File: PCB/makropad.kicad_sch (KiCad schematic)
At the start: 46 parts, among them J1 OLED_DISPLAY, J2 Conn_01x04, SW1 SW_Push_45deg, SW10 SW_Push_45deg, SW11 RotaryEncoder_Switch, SW12 RotaryEncoder_Switch, SW2 SW_Push_45deg, SW3 SW_Push_45deg, SW4 SW_Push_45deg, SW5 SW_Push_45deg, SW6 SW_Push_45deg, SW7 SW_Push_45deg, SW8 SW_Push_45deg, SW9 SW_Push_45deg, U1 PCF8574A, U2 MOUDLE-SEEEDUINO-XIAO

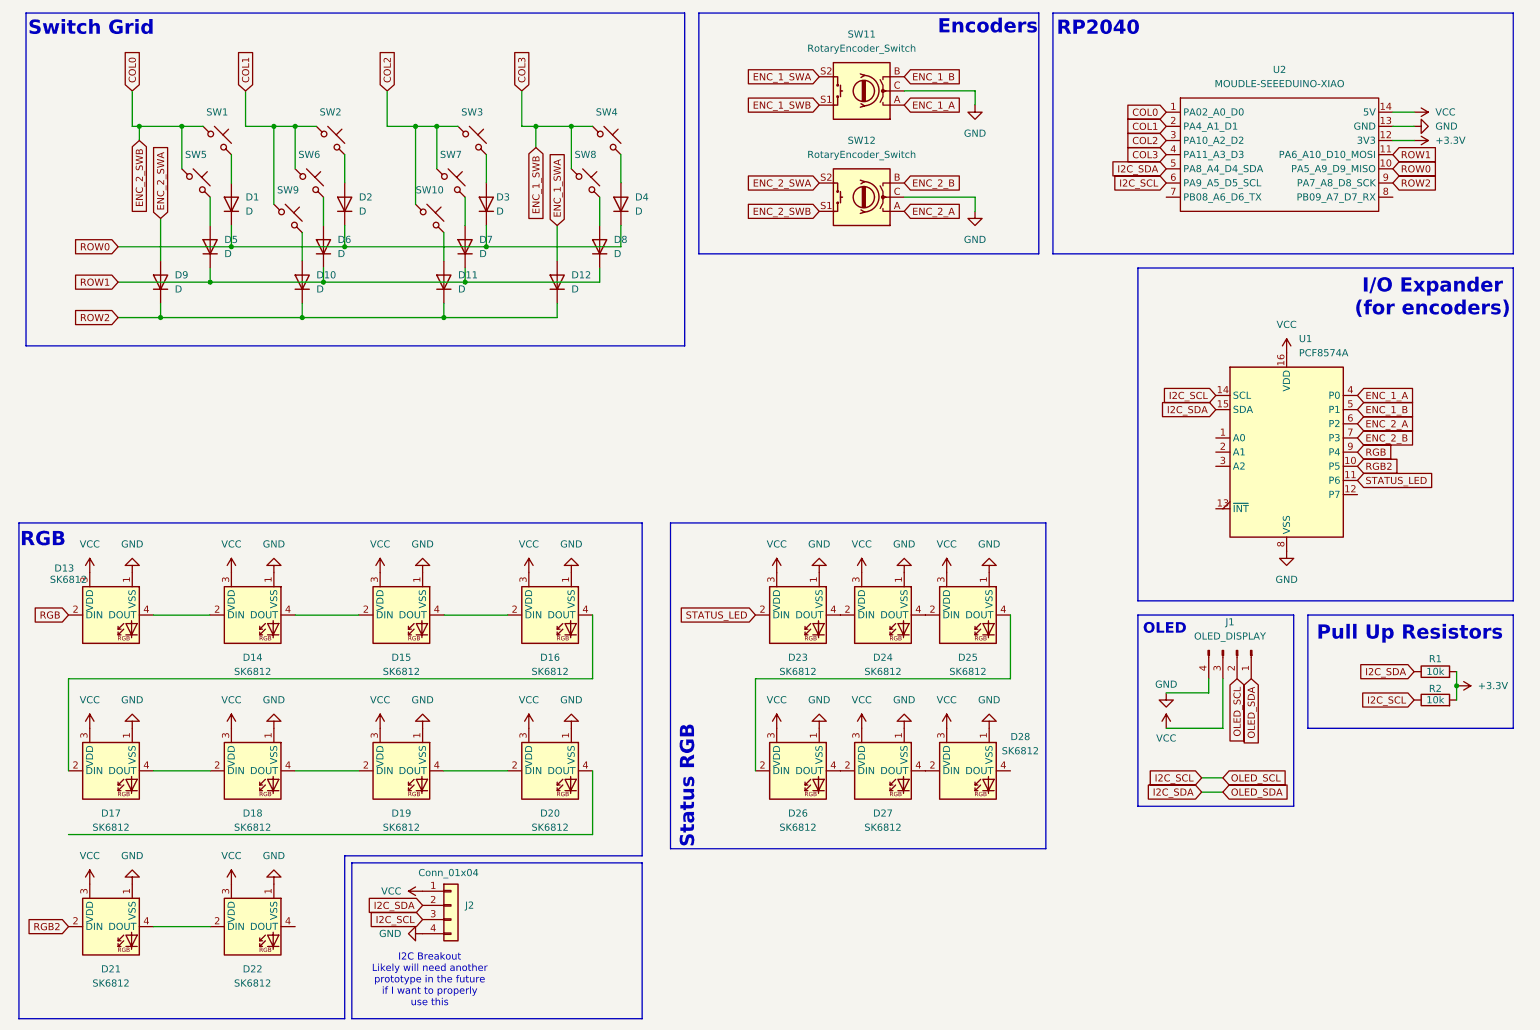
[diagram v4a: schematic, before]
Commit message: finally finish up pcb and fix led wiring
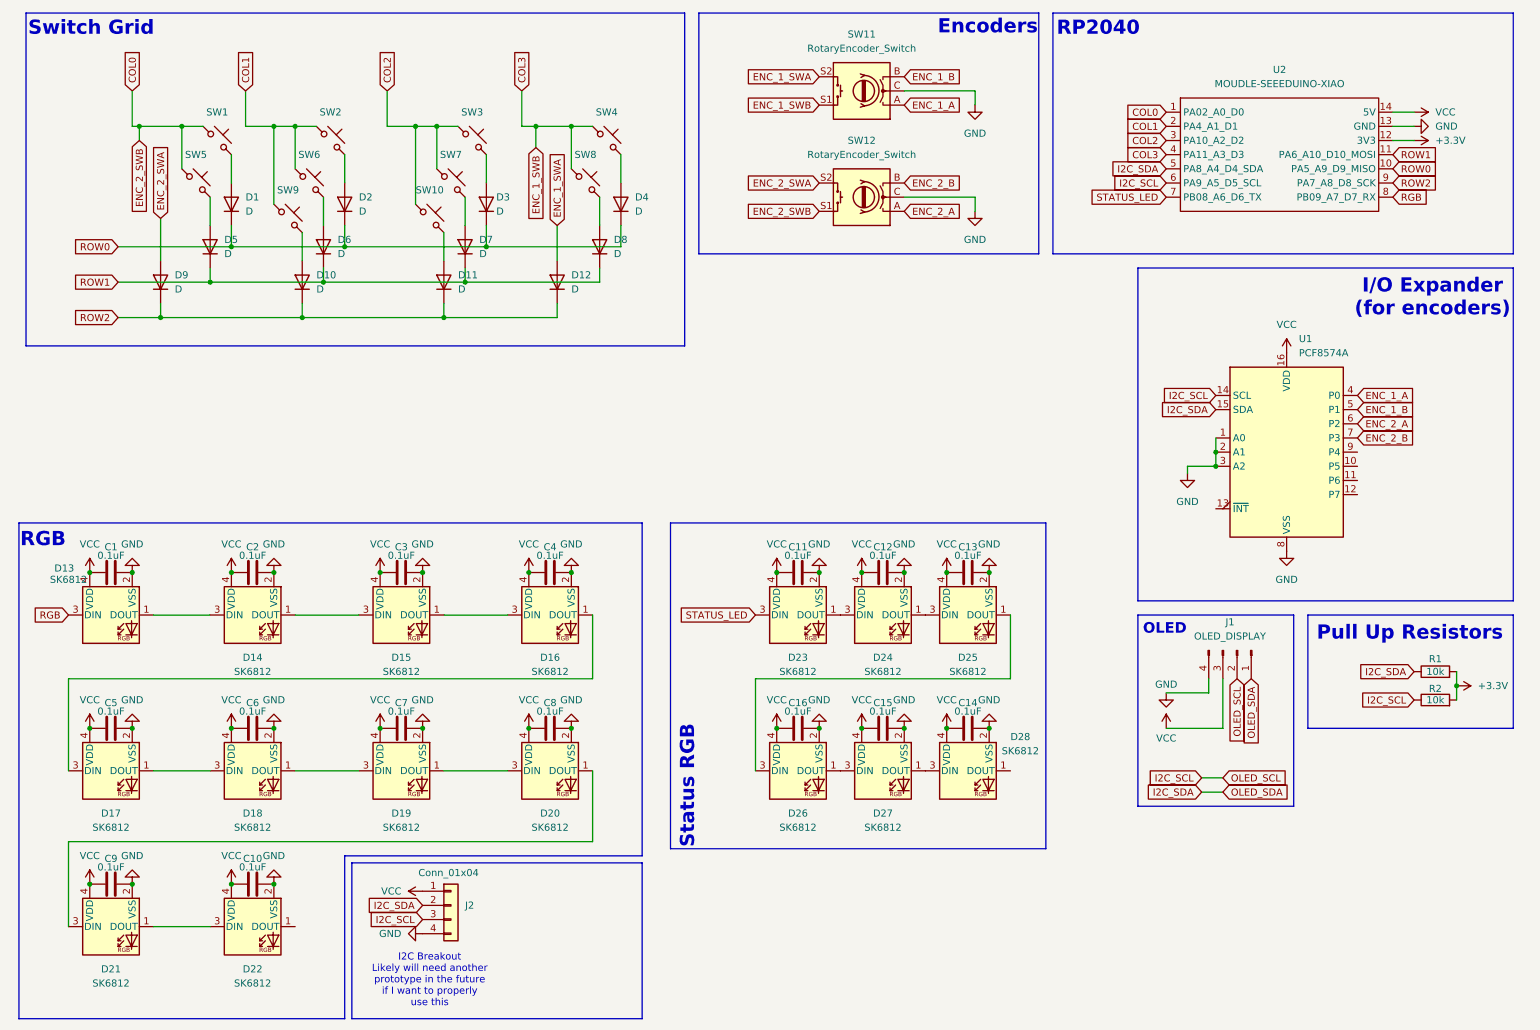
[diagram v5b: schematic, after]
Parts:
- added C1, C10, C11, C12, C13, C14, C15, C16, C2, C3, C4, C5, C6, C7, C8, C9: 0.1uF, Capacitor_SMD:C_1206_3216Metric, symbol Device:C
- D13, D14, D15, D16, D17, D18, D19, D20, D21, D22: footprint Components:LED_SK6812MINI -> neopixel.petty:SK6812MINI-E; symbol SK6812_CUSTOM:SK6812_Custom -> neopixel:SK6812MINI
- D23, D24, D25, D26, D27, D28: footprint LED_SMD:LED_SK6812_PLCC4_5.0x5.0mm_P3.2mm -> LED_SMD:LED_SK6812MINI_PLCC4_3.5x3.5mm_P1.75mm; symbol SK6812_CUSTOM:SK6812_Custom -> neopixel:SK6812MINI
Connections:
- net GND: now also D13.2 (VSS), D14.2 (VSS), D15.2 (VSS), D16.2 (VSS), D17.2 (VSS), D18.2 (VSS), D19.2 (VSS), D20.2 (VSS), D21.2 (VSS), D22.2 (VSS), D23.2 (VSS), D24.2 (VSS), D25.2 (VSS), D26.2 (VSS), D27.2 (VSS), D28.2 (VSS), U1.1 (A0), U1.2 (A1), U1.3 (A2), C1.2, C10.2, C11.2, C12.2, C13.2, C14.2, C15.2, C16.2, C2.2, C3.2, C4.2, C5.2, C6.2, C7.2, C8.2, C9.2; no longer D13.1 (VSS), D14.1 (VSS), D15.1 (VSS), D16.1 (VSS), D17.1 (VSS), D18.1 (VSS), D19.1 (VSS), D20.1 (VSS), D21.1 (VSS), D22.1 (VSS), D23.1 (VSS), D24.1 (VSS), D25.1 (VSS), D26.1 (VSS), D27.1 (VSS), D28.1 (VSS)
- net RGB: now also D13.3 (DIN), U2.8 (PB09_A7_D7_RX); no longer D13.2 (DIN), U1.9 (P4)
- net STATUS_LED: now also D23.3 (DIN), U2.7 (PB08_A6_D6_TX); no longer D23.2 (DIN), U1.11 (P6)
- net VCC: now also D13.4 (VDD), D14.4 (VDD), D15.4 (VDD), D16.4 (VDD), D17.4 (VDD), D18.4 (VDD), D19.4 (VDD), D20.4 (VDD), D21.4 (VDD), D22.4 (VDD), D23.4 (VDD), D24.4 (VDD), D25.4 (VDD), D26.4 (VDD), D27.4 (VDD), D28.4 (VDD), C1.1, C10.1, C11.1, C12.1, C13.1, C14.1, C15.1, C16.1, C2.1, C3.1, C4.1, C5.1, C6.1, C7.1, C8.1, C9.1; no longer D13.3 (VDD), D14.3 (VDD), D15.3 (VDD), D16.3 (VDD), D17.3 (VDD), D18.3 (VDD), D19.3 (VDD), D20.3 (VDD), D21.3 (VDD), D22.3 (VDD), D23.3 (VDD), D24.3 (VDD), D25.3 (VDD), D26.3 (VDD), D27.3 (VDD), D28.3 (VDD)
- net RGB2: no longer names the net of U1.10 (P5)
- net RGB2: no longer D21.2 (DIN)
- new net: D27.1 (DOUT), D28.3 (DIN)
- new net: D14.1 (DOUT), D15.3 (DIN)
- new net: D13.1 (DOUT), D14.3 (DIN)
- new net: D18.1 (DOUT), D19.3 (DIN)
- new net: D17.1 (DOUT), D18.3 (DIN)
- new net: D21.1 (DOUT), D22.3 (DIN)
- new net: D20.1 (DOUT), D21.3 (DIN)
- new net: D26.1 (DOUT), D27.3 (DIN)
- new net: D19.1 (DOUT), D20.3 (DIN)
- new net: D25.1 (DOUT), D26.3 (DIN)
- new net: D16.1 (DOUT), D17.3 (DIN)
- new net: D15.1 (DOUT), D16.3 (DIN)
- new net: D24.1 (DOUT), D25.3 (DIN)
- new net: D23.1 (DOUT), D24.3 (DIN)
